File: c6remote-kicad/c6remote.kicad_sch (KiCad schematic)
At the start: 29 parts, among them J1 Battery, Q1 MMBT2222A, SW1 SW_Push, SW10 SW_Push, SW11 SW_Push, SW2 SW_Push, SW3 SW_Push, SW4 SW_Push, SW5 SW_Push, SW6 SW_Push, SW7 SW_Push, SW8 SW_Push, SW9 SW_Push, U1 XIAO-ESP32-C6, U2 TSOP45xx, U3 PCF8575DBR

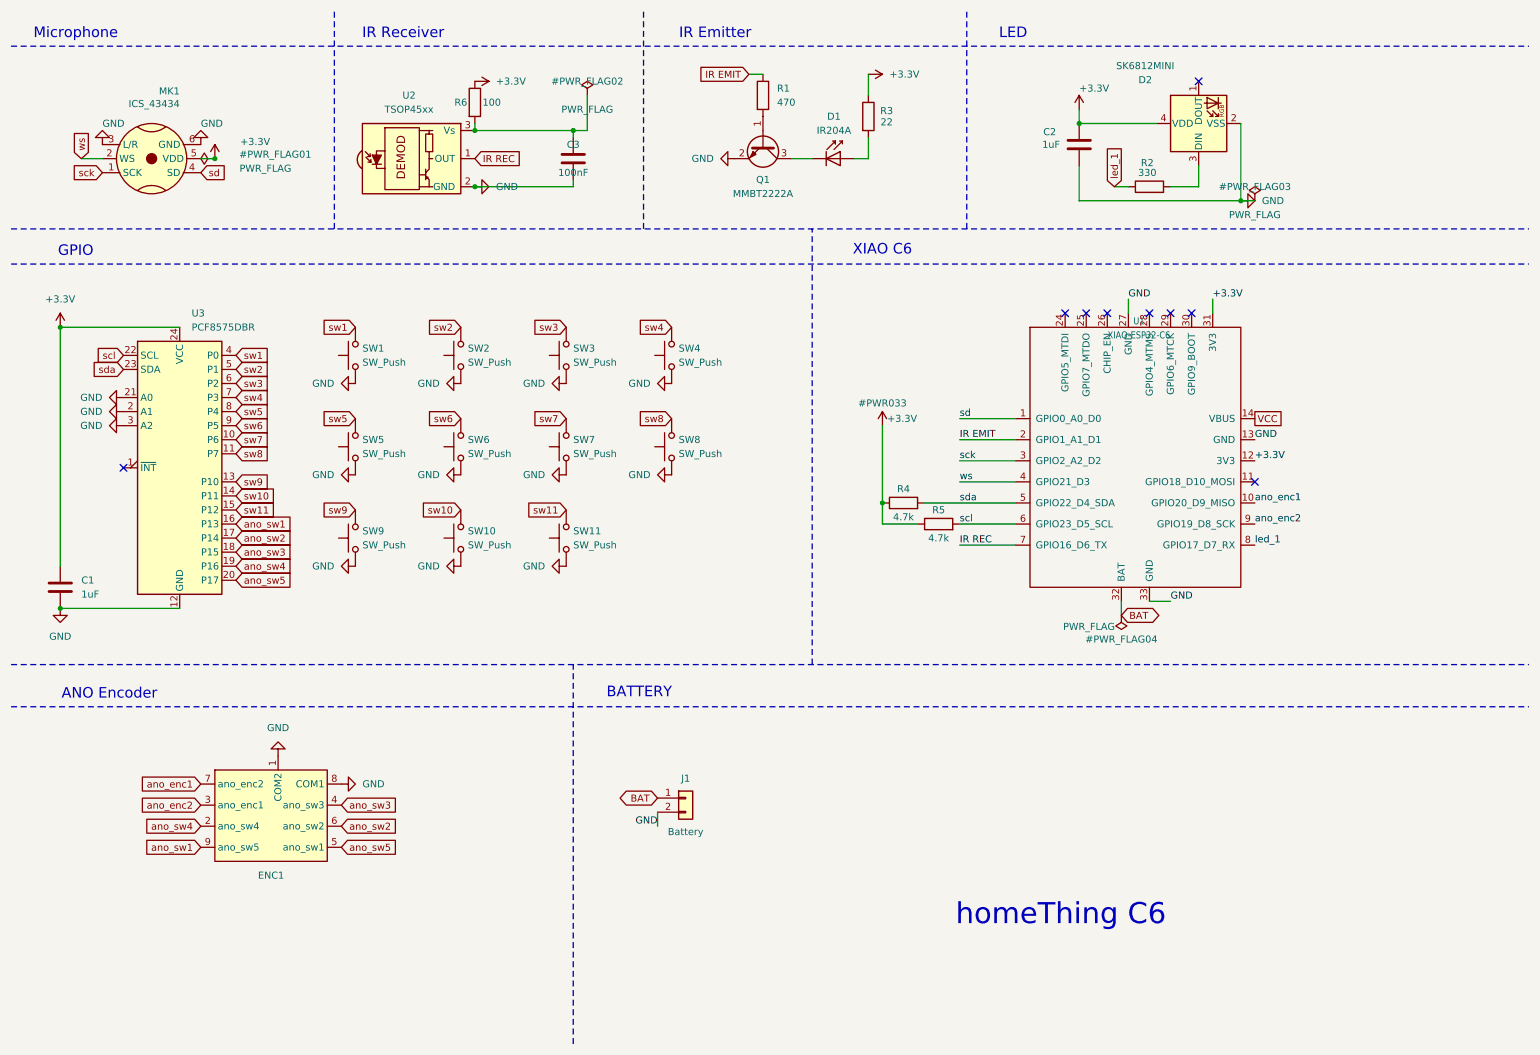
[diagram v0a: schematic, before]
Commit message: fix(bom): swap PCBWay out-of-stock parts - D1 IR204-A->Inolux INL-3AHIR30 (3mm 940nm 100mA radial, matches ~80mA drive via R3/+3.3V, keeps 90deg lead-form at assembly), U2 TSOP4536->Vishay TSOP4136 (36kHz 2.5-5.5V, same MOLD-3 footprint/pinout, in stock), ENC1 Adafruit 5001 marked DNP (no equivalent, hand-solder later); update schematic Value/datasheet + dnp flag and BOM CSV; netlist connectivity + ERC/DRC baselines unchanged
Co-Authored-By: Claude Opus 4.8 (1M context) <noreply@anthropic.com>
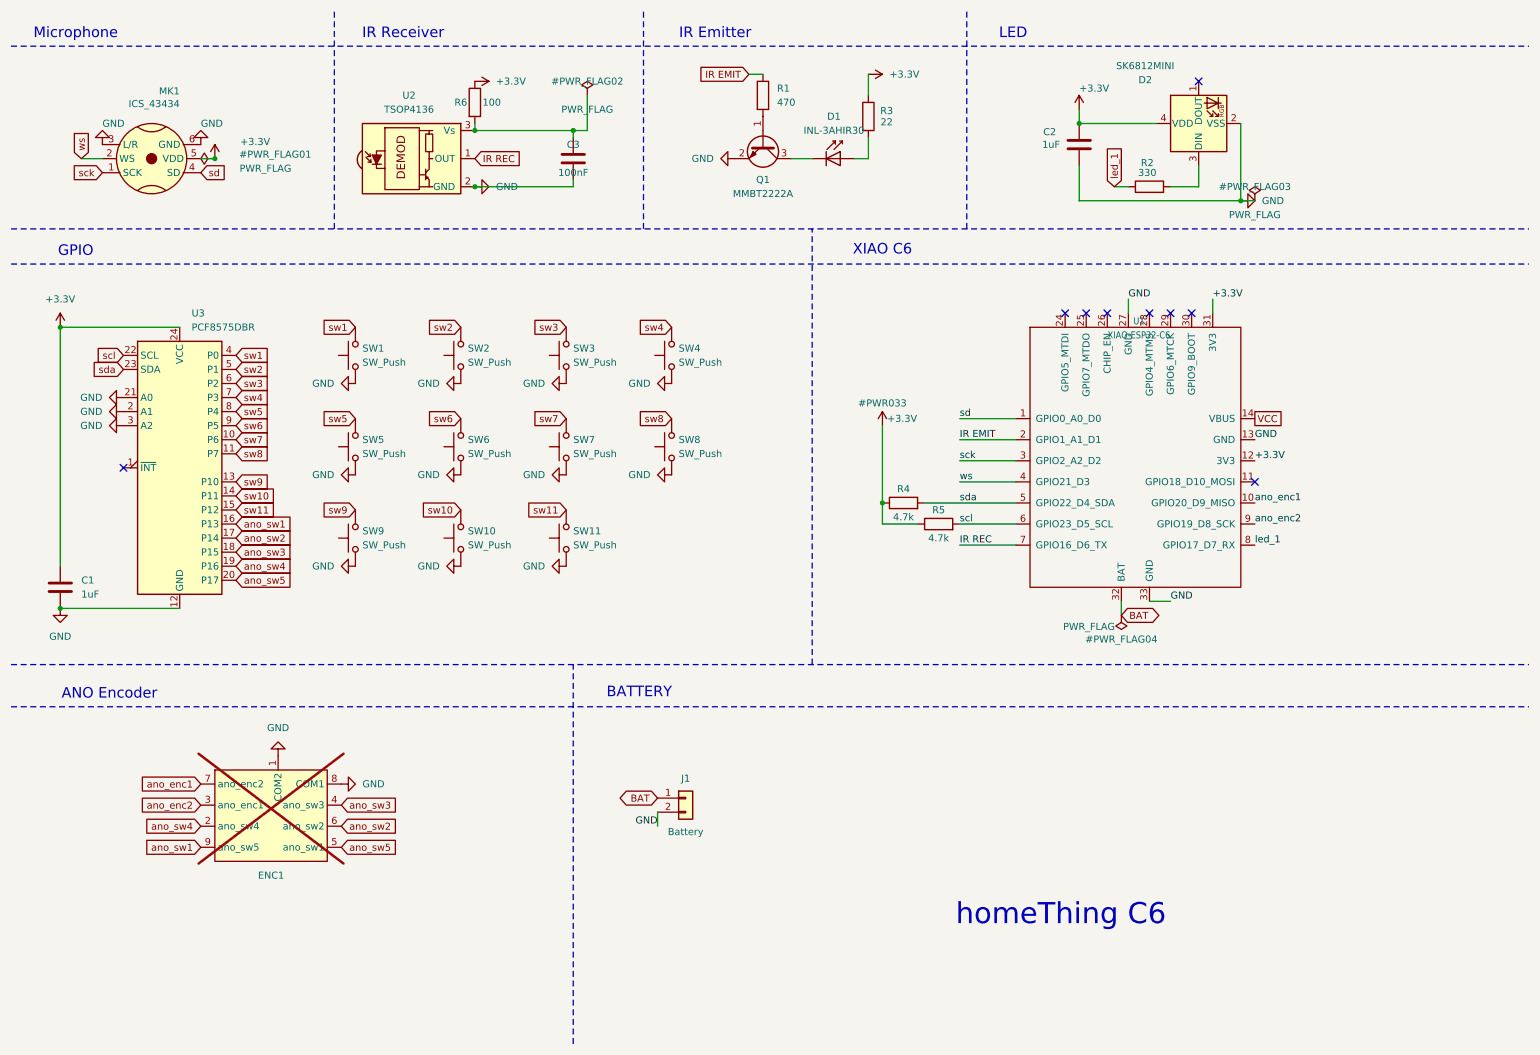
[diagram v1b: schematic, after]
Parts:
- D1: value IR204A -> INL-3AHIR30
- ENC1: now not fitted
- U2: value TSOP45xx -> TSOP4136
